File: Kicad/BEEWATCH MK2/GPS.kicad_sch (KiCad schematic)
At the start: 12 parts

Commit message: Schematic changes
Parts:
- R11, R12, R13, R14, R15, R16, R42: footprint Resistor_SMD:R_0402_1005Metric -> Resistor_SMD:R_0402_1005Metric_Pad0.72x0.64mm_HandSolder
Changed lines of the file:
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@@
 			)
 		)
-		(property "Footprint" "Resistor_SMD:R_0402_1005Metric"
+		(property "Footprint" "Resistor_SMD:R_0402_1005Metric_Pad0.72x0.64mm_HandSolder"
 			(at 167.64 92.71 0)
 			(effects
@@
 			)
 		)
-		(property "Footprint" "Resistor_SMD:R_0402_1005Metric"
+		(property "Footprint" "Resistor_SMD:R_0402_1005Metric_Pad0.72x0.64mm_HandSolder"
 			(at 175.26 92.71 0)
 			(effects
@@
 			)
 		)
-		(property "Footprint" "Resistor_SMD:R_0402_1005Metric"
+		(property "Footprint" "Resistor_SMD:R_0402_1005Metric_Pad0.72x0.64mm_HandSolder"
 			(at 91.44 91.44 0)
 			(effects
@@
 			)
 		)
-		(property "Footprint" "Resistor_SMD:R_0402_1005Metric"
+		(property "Footprint" "Resistor_SMD:R_0402_1005Metric_Pad0.72x0.64mm_HandSolder"
 			(at 115.57 114.3 0)
 			(effects
@@
 			)
 		)
-		(property "Footprint" "Resistor_SMD:R_0402_1005Metric"
+		(property "Footprint" "Resistor_SMD:R_0402_1005Metric_Pad0.72x0.64mm_HandSolder"
 			(at 97.79 91.44 0)
 			(effects
@@
 			)
 		)
-		(property "Footprint" "Resistor_SMD:R_0402_1005Metric"
+		(property "Footprint" "Resistor_SMD:R_0402_1005Metric_Pad0.72x0.64mm_HandSolder"
 			(at 115.57 111.76 0)
 			(effects
@@
 			)
 		)
-		(property "Footprint" "Resistor_SMD:R_0402_1005Metric"
+		(property "Footprint" "Resistor_SMD:R_0402_1005Metric_Pad0.72x0.64mm_HandSolder"
 			(at 115.57 104.14 0)
 			(effects

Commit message: Updated to KiCad 9!
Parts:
- gave numbers to parts that had none: 1

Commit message: ERC Checking
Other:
- moved on the sheet: C14, C15, C16, C17, R11, R12, R13, R14, R15, R16, R42, U3

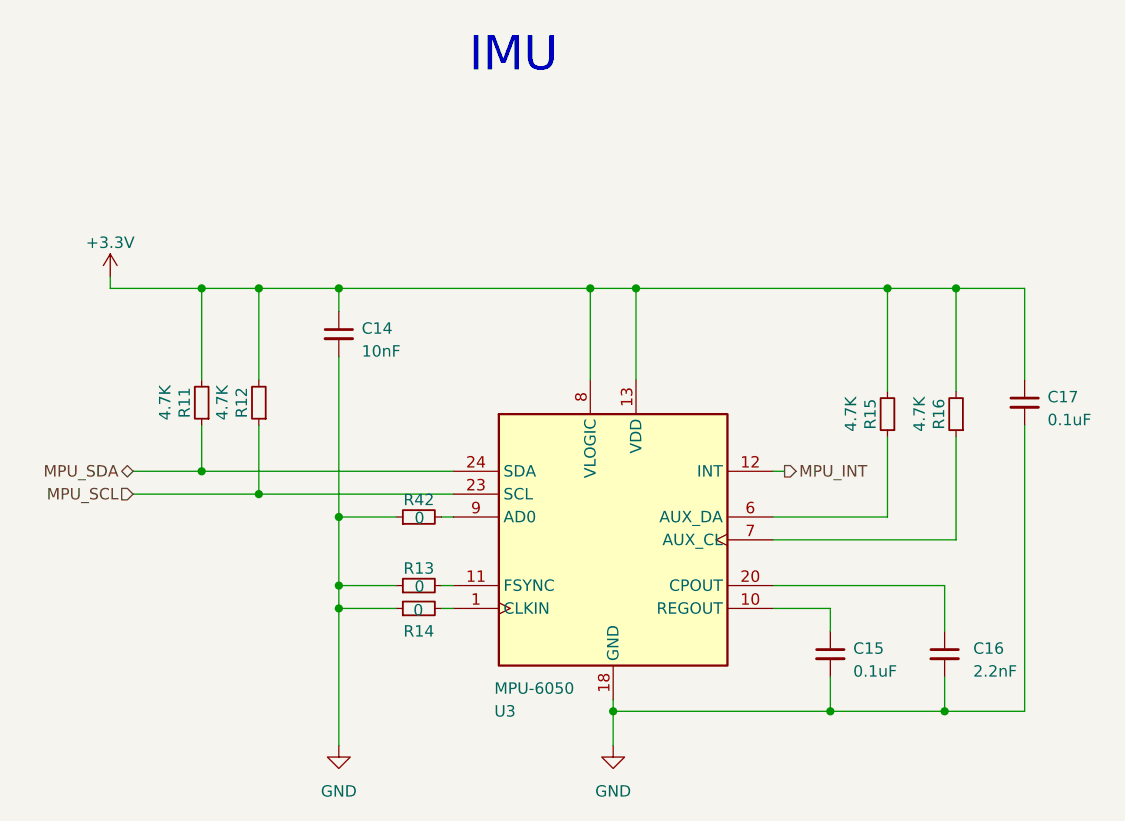
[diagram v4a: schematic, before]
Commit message: Updating MPN
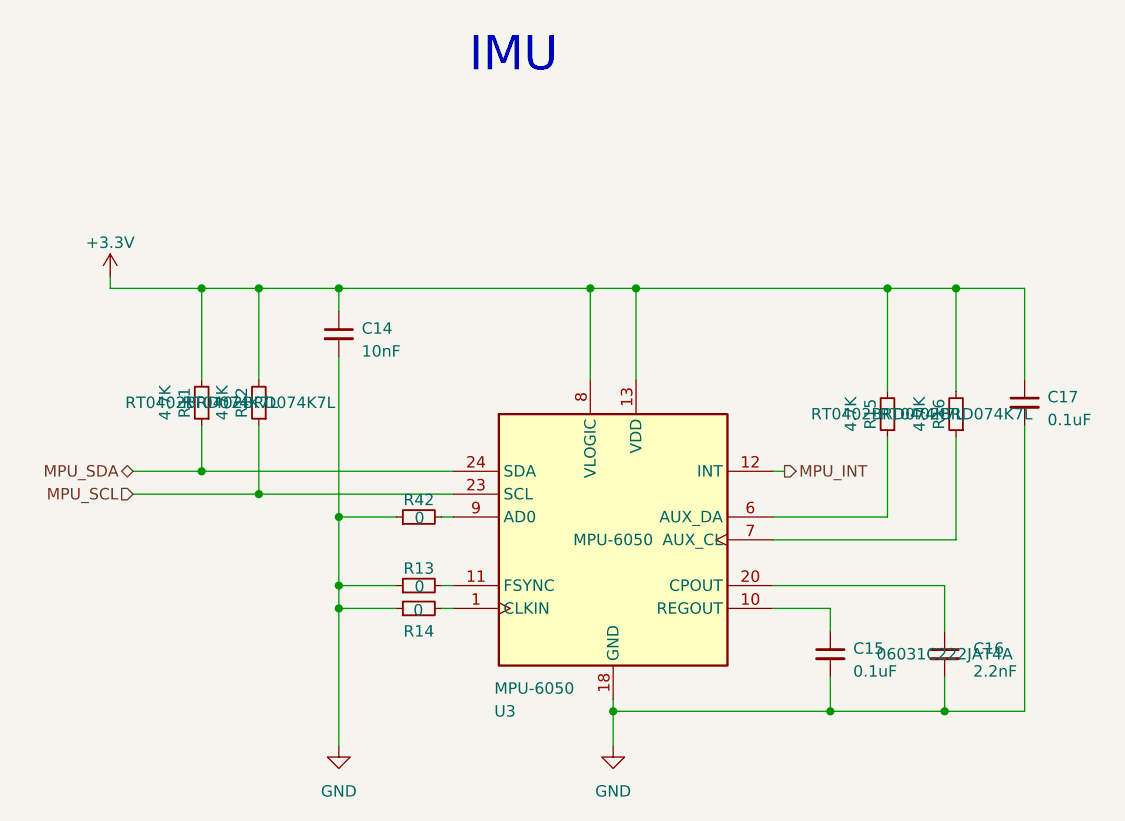
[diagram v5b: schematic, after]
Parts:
- C16: MPN (none) -> 06031C222JAT4A
- R11, R12, R15, R16: MPN (none) -> RT0402BRD074K7L
- U3: MPN (none) -> MPU-6050
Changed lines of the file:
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@@
 			)
 		)
-		(property "MPN" ""
+		(property "MPN" "06031C222JAT4A "
 			(at 175.26 120.65 0)
 			(effects
@@
 			)
 		)
-		(property "MPN" ""
+		(property "MPN" "RT0402BRD074K7L"
 			(at 168.91 93.98 0)
 			(effects
@@
 			)
 		)
-		(property "MPN" ""
+		(property "MPN" "RT0402BRD074K7L"
 			(at 176.53 93.98 0)
 			(effects
@@
 			)
 		)
-		(property "MPN" ""
+		(property "MPN" "RT0402BRD074K7L"
 			(at 92.71 92.71 0)
 			(effects
@@
 			)
 		)
-		(property "MPN" ""
+		(property "MPN" "MPU-6050"
 			(at 138.43 107.95 0)
 			(effects
@@
 			)
 		)
-		(property "MPN" ""
+		(property "MPN" "RT0402BRD074K7L"
 			(at 99.06 92.71 0)
 			(effects
